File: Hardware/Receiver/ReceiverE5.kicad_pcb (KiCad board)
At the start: 2 copper layers, 41 parts, among them J1 KBUS, J2 AVR-PDI-6A, J3 CONN_01X08, J4 CONN_01X06, J5 CONN_01X06, J6 CONN_01X04, J7 CONN_01X04, U1 ATXMEGA32E5-A, U2 LM2731, U3 SN74LV07A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

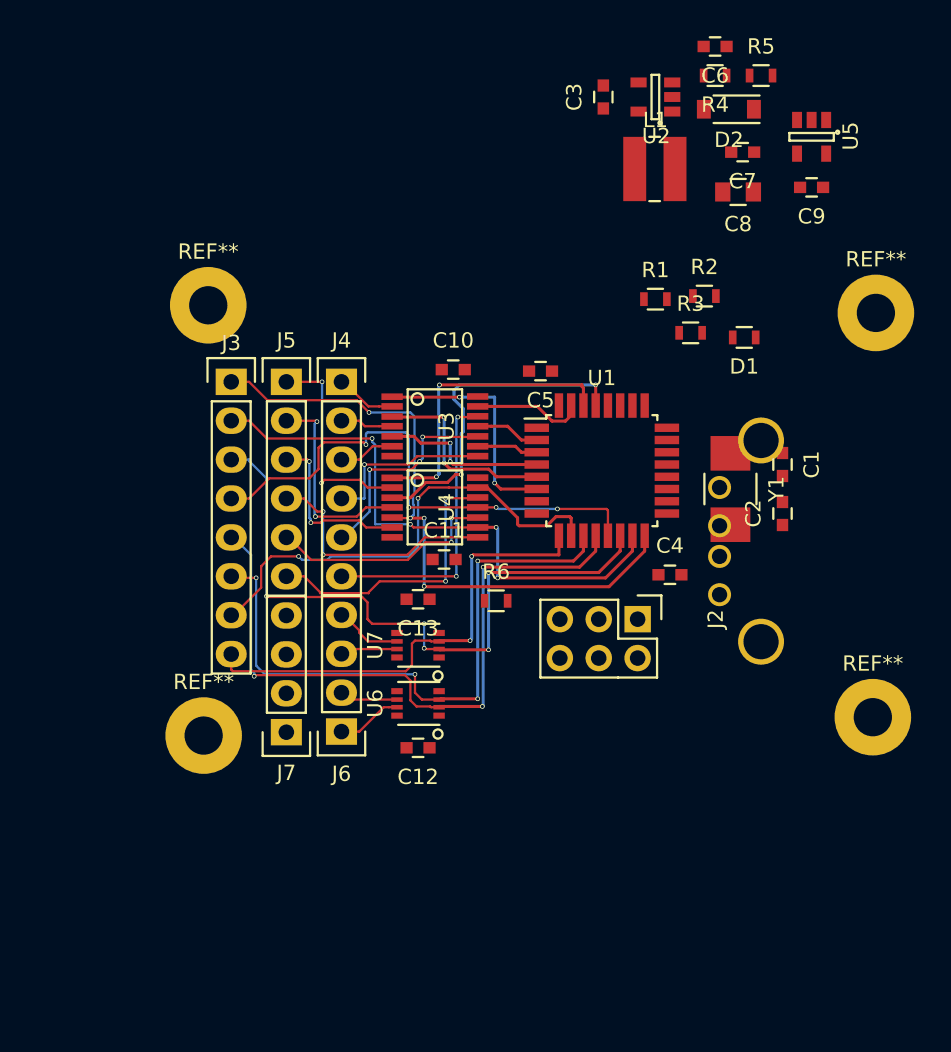
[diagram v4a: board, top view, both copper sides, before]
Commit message: 50x30mm layout
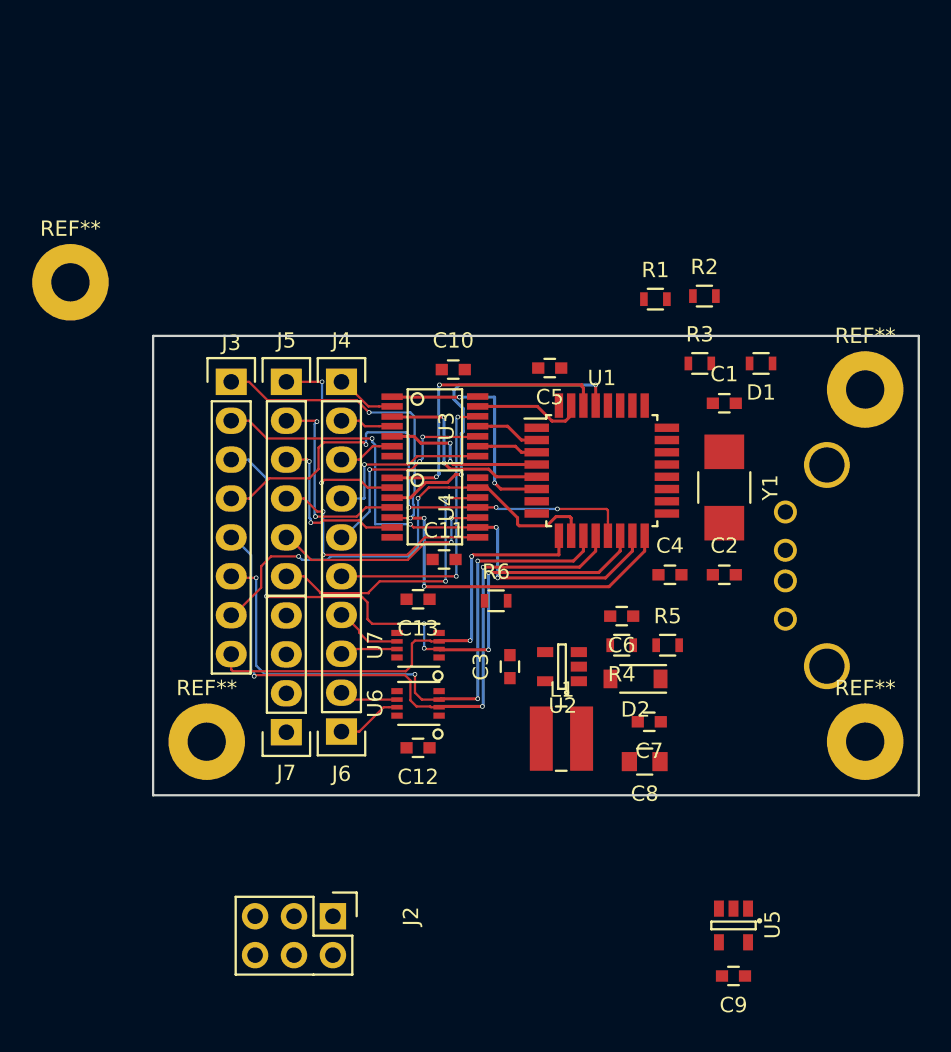
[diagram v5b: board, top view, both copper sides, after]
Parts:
- moved C9 51.8 mm to (104.9, 104.8)
- moved U5 51.8 mm to (104.9, 101.5)
- moved R4 37.7 mm to (97.6, 83.2)
- moved R5 37.7 mm to (100.6, 83.2)
- moved C3 37.7 mm to (90.3, 84.6)
- moved C6 37.7 mm to (97.6, 81.3)
- moved C7 37.7 mm to (99.4, 88.2)
- moved C8 37.7 mm to (99.1, 90.8)
- moved D2 37.7 mm to (98.5, 85.4)
- moved L1 37.7 mm to (93.7, 89.3)
- moved U2 37.7 mm to (93.7, 84.6)
- moved J2 27.8 mm to (78.7, 100.9)
- moved REF** 9.12 mm to (61.6, 59.5)
- moved C1 5.52 mm to (104.3, 67.4), turned to 0 degrees
- moved C2 5.52 mm to (104.3, 78.6), turned to 0 degrees
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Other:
- board outline added: 50 x 30 mm
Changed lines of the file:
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@@
     (area 0 0 0 0)
     (thickness 1.6)
-    (drawings 1)
+    (drawings 7)
     (tracks 369)
     (zones 0)
@@
   )
   (module Mounting_Holes:MountingHole_2.5mm_Pad (layer F.Cu)
-    (at 114.2 61.5)
+    (at 113.5 66.5)
     (descr "Mounting Hole 2.5mm")
     (tags "mounting hole 2.5mm")
@@
   )
   (module Mounting_Holes:MountingHole_2.5mm_Pad (layer F.Cu)
-    (at 114 87.9)
+    (at 113.5 89.5)
     (descr "Mounting Hole 2.5mm")
     (tags "mounting hole 2.5mm")
@@
   )
   (module Mounting_Holes:MountingHole_2.5mm_Pad (layer F.Cu)
-    (at 70.3 89.1)
+    (at 70.5 89.5)
     (descr "Mounting Hole 2.5mm")
     (tags "mounting hole 2.5mm")
@@
   )
   (module Capacitors_SMD:C_0603 (layer F.Cu)
-    (at 108.1 71.4 270)
+    (at 104.3 67.4)
     (descr "Capacitor SMD 0603, reflow soldering, AVX (see smccp.pdf)")
     (tags "capacitor 0603")
     (attr smd)
-    (fp_text reference C1 (at 0 -1.9 270) (layer F.SilkS)
-      (effects (font (size 1 1) (thickness 0.15)))
-    )
-    (fp_text value 22p (at 0 1.9 270) (layer F.Fab)
+    (fp_text reference C1 (at 0 -1.9) (layer F.SilkS)
+      (effects (font (size 1 1) (thickness 0.15)))
+    )
+    (fp_text value 22p (at 0 1.9) (layer F.Fab)
       (effects (font (size 1 1) (thickness 0.15)))
     )
@@
     (fp_line (start -0.35 -0.6) (end 0.35 -0.6) (layer F.SilkS) (width 0.15))
     (fp_line (start 0.35 0.6) (end -0.35 0.6) (layer F.SilkS) (width 0.15))
-    (pad 1 smd rect (at -0.75 0 270) (size 0.8 0.75) (layers F.Cu F.Paste F.Mask)
+    (pad 1 smd rect (at -0.75 0) (size 0.8 0.75) (layers F.Cu F.Paste F.Mask)
       (net 1 "Net-(C1-Pad1)"))
-    (pad 2 smd rect (at 0.75 0 270) (size 0.8 0.75) (layers F.Cu F.Paste F.Mask)
+    (pad 2 smd rect (at 0.75 0) (size 0.8 0.75) (layers F.Cu F.Paste F.Mask)
       (net 2 GND))
     (model Capacitors_SMD.3dshapes/C_0603.wrl
@@
   )
   (module Capacitors_SMD:C_0603 (layer F.Cu)
-    (at 108.1 74.6 90)
+    (at 104.3 78.6)
     (descr "Capacitor SMD 0603, reflow soldering, AVX (see smccp.pdf)")
     (tags "capacitor 0603")
     (attr smd)
-    (fp_text reference C2 (at 0 -1.9 90) (layer F.SilkS)
-      (effects (font (size 1 1) (thickness 0.15)))
-    )
-    (fp_text value 22p (at 0 1.9 90) (layer F.Fab)
+    (fp_text reference C2 (at 0 -1.9) (layer F.SilkS)
+      (effects (font (size 1 1) (thickness 0.15)))
+    )
+    (fp_text value 22p (at 0 1.9) (layer F.Fab)
       (effects (font (size 1 1) (thickness 0.15)))
     )
@@
     (fp_line (start -0.35 -0.6) (end 0.35 -0.6) (layer F.SilkS) (width 0.15))
     (fp_line (start 0.35 0.6) (end -0.35 0.6) (layer F.SilkS) (width 0.15))
-    (pad 1 smd rect (at -0.75 0 90) (size 0.8 0.75) (layers F.Cu F.Paste F.Mask)
+    (pad 1 smd rect (at -0.75 0) (size 0.8 0.75) (layers F.Cu F.Paste F.Mask)
       (net 3 "Net-(C2-Pad1)"))
-    (pad 2 smd rect (at 0.75 0 90) (size 0.8 0.75) (layers F.Cu F.Paste F.Mask)
+    (pad 2 smd rect (at 0.75 0) (size 0.8 0.75) (layers F.Cu F.Paste F.Mask)
       (net 2 GND))
     (model Capacitors_SMD.3dshapes/C_0603.wrl
@@
   )
   (module Capacitors_SMD:C_0603 (layer F.Cu)
-    (at 96.4 47.4 90)
+    (at 90.3 84.6 90)
     (descr "Capacitor SMD 0603, reflow soldering, AVX (see smccp.pdf)")
     (tags "capacitor 0603")
@@
   )
   (module Capacitors_SMD:C_0603 (layer F.Cu)
-    (at 92.3 65.3 180)
+    (at 92.9 65.1 180)
     (descr "Capacitor SMD 0603, reflow soldering, AVX (see smccp.pdf)")
     (tags "capacitor 0603")
@@
   )
   (module Capacitors_SMD:C_0603 (layer F.Cu)
-    (at 103.7 44.1 180)
+    (at 97.6 81.3 180)
     (descr "Capacitor SMD 0603, reflow soldering, AVX (see smccp.pdf)")
     (tags "capacitor 0603")
@@
   )
   (module Capacitors_SMD:C_0603 (layer F.Cu)
-    (at 105.5 51 180)
+    (at 99.4 88.2 180)
     (descr "Capacitor SMD 0603, reflow soldering, AVX (see smccp.pdf)")
     (tags "capacitor 0603")
@@
   )
   (module Capacitors_SMD:C_0805 (layer F.Cu)
-    (at 105.2 53.6 180)
+    (at 99.1 90.8 180)
     (descr "Capacitor SMD 0805, reflow soldering, AVX (see smccp.pdf)")
     (tags "capacitor 0805")
@@
   )
   (module Capacitors_SMD:C_0603 (layer F.Cu)
-    (at 110 53.3 180)
+    (at 104.9 104.8 180)
     (descr "Capacitor SMD 0603, reflow soldering, AVX (see smccp.pdf)")
     (tags "capacitor 0603")
@@
   )
   (module Resistors_SMD:R_0603 (layer F.Cu)
-    (at 105.6 63.1 180)
+    (at 106.7 64.8 180)
     (descr "Resistor SMD 0603, reflow soldering, Vishay (see dcrcw.pdf)")
     (tags "resistor 0603")
@@
   )
   (module Diodes_SMD:SOD-123 (layer F.Cu)
-    (at 104.6 48.2 180)
+    (at 98.5 85.4 180)
     (descr SOD-123)
     (tags SOD-123)
@@
   )
   (module kuro:USB_A_multicomp (layer B.Cu)
-    (at 106.7 76.4 270)
+    (at 111 78 270)
     (descr "FCI 87520")
     (tags "USB USB_A")
@@
   )
   (module Pin_Headers:Pin_Header_Straight_2x03 (layer F.Cu)
-    (at 98.64 81.5 270)
+    (at 78.74 100.9 270)
     (descr "Through hole pin header")
     (tags "pin header")
@@
   )
   (module kuro:SRN4012TA (layer F.Cu)
-    (at 99.8 52.1)
+    (at 93.7 89.3)
     (descr http://www.farnell.com/datasheets/2113222.pdf)
     (tags "Bournes inductor")
@@
   )
   (module Resistors_SMD:R_0603 (layer F.Cu)
-    (at 102.1 62.8)
+    (at 102.7 64.8)
     (descr "Resistor SMD 0603, reflow soldering, Vishay (see dcrcw.pdf)")
     (tags "resistor 0603")
@@
   )
   (module Resistors_SMD:R_0603 (layer F.Cu)
-    (at 103.7 46 180)
+    (at 97.6 83.2 180)
     (descr "Resistor SMD 0603, reflow soldering, Vishay (see dcrcw.pdf)")
     (tags "resistor 0603")
@@
   )
   (module Resistors_SMD:R_0603 (layer F.Cu)
-    (at 106.7 46)
+    (at 100.6 83.2)
     (descr "Resistor SMD 0603, reflow soldering, Vishay (see dcrcw.pdf)")
     (tags "resistor 0603")
@@
   )
   (module TO_SOT_Packages_SMD:SOT-23-5 (layer F.Cu)
-    (at 99.8 47.4 180)
+    (at 93.7 84.6 180)
     (descr "5-pin SOT23 package")
     (tags SOT-23-5)
@@
   )
   (module TO_SOT_Packages_SMD:SOT-23-5 (layer F.Cu)
-    (at 110 50 270)
+    (at 104.9 101.5 270)
     (descr "5-pin SOT23 package")
     (tags SOT-23-5)
@@
   )
   (module kuro:SMD_Crystal_Multi_QC6CB_7A_ABM7 (layer F.Cu)
-    (at 104.7 73 270)
+    (at 104.3 72.9 270)
     (descr "Multiple SMD crystal footprint.svg")
     (tags "QC6CB 7A ABM7")
@@
   )
   (module Mounting_Holes:MountingHole_2.5mm_Pad (layer F.Cu)
-    (at 70.6 61)
+    (at 61.6 59.5)
     (descr "Mounting Hole 2.5mm")
     (tags "mounting hole 2.5mm")
@@
     (pad 1 thru_hole circle (at 0 0) (size 5 5) (drill 2.5) (layers *.Cu *.Mask))
   )
-  (dimension 50 (width 0.3) (layer Eco1.User)
-    (gr_text "50.000 mm" (at 95.086733 49.844833) (layer Eco1.User)
+  (dimension 15 (width 0.3) (layer F.Fab)
+    (gr_text "15.000 mm" (at 122.017914 70.522279 270) (layer F.Fab)
       (effects (font (size 1.5 1.5) (thickness 0.3)))
     )
-    (feature1 (pts (xy 120.086733 49.844833) (xy 120.086733 49.844833)))
-    (feature2 (pts (xy 70.086733 49.844833) (xy 70.086733 49.844833)))
-    (crossbar (pts (xy 70.086733 49.844833) (xy 120.086733 49.844833)))
-    (arrow1a (pts (xy 120.086733 49.844833) (xy 118.960229 50.431254)))
-    (arrow1b (pts (xy 120.086733 49.844833) (xy 118.960229 49.258412)))
-    (arrow2a (pts (xy 70.086733 49.844833) (xy 71.213237 50.431254)))
-    (arrow2b (pts (xy 70.086733 49.844833) (xy 71.213237 49.258412)))
-  )
+    (feature1 (pts (xy 122.017914 78.022279) (xy 122.017914 78.022279)))
+    (feature2 (pts (xy 122.017914 63.022279) (xy 122.017914 63.022279)))
+    (crossbar (pts (xy 122.017914 63.022279) (xy 122.017914 78.022279)))
+    (arrow1a (pts (xy 122.017914 78.022279) (xy 121.431493 76.895775)))
+    (arrow1b (pts (xy 122.017914 78.022279) (xy 122.604335 76.895775)))
+    (arrow2a (pts (xy 122.017914 63.022279) (xy 121.431493 64.148783)))
+    (arrow2b (pts (xy 122.017914 63.022279) (xy 122.604335 64.148783)))
+  )
+  (dimension 30 (width 0.3) (layer F.Fab)
+    (gr_text "30.000 mm" (at 65 78 270) (layer F.Fab)
+      (effects (font (size 1.5 1.5) (thickness 0.3)))
+    )
+    (feature1 (pts (xy 65 93) (xy 65 93)))
+    (feature2 (pts (xy 65 63) (xy 65 63)))
+    (crossbar (pts (xy 65 63) (xy 65 93)))
+    (arrow1a (pts (xy 65 93) (xy 64.413579 91.873496)))
+    (arrow1b (pts (xy 65 93) (xy 65.586421 91.873496)))
+    (arrow2a (pts (xy 65 63) (xy 64.413579 64.126504)))
+    (arrow2b (pts (xy 65 63) (xy 65.586421 64.126504)))
+  )
+  (dimension 50 (width 0.3) (layer F.Fab)
+    (gr_text "50.000 mm" (at 92 61) (layer F.Fab)
+      (effects (font (size 1.5 1.5) (thickness 0.3)))
+    )
+    (feature1 (pts (xy 67 61) (xy 67 61)))
+    (feature2 (pts (xy 117 61) (xy 117 61)))
+    (crossbar (pts (xy 117 61) (xy 67 61)))
+    (arrow1a (pts (xy 67 61) (xy 68.126504 60.413579)))
+    (arrow1b (pts (xy 67 61) (xy 68.126504 61.586421)))
+    (arrow2a (pts (xy 117 61) (xy 115.873496 60.413579)))
+    (arrow2b (pts (xy 117 61) (xy 115.873496 61.586421)))
+  )
+  (gr_line (start 67 63) (end 67 93) (layer Edge.Cuts) (width 0.15))
+  (gr_line (start 117 63) (end 67 63) (layer Edge.Cuts) (width 0.15))
+  (gr_line (start 117 93) (end 117 63) (layer Edge.Cuts) (width 0.15))
+  (gr_line (start 67 93) (end 117 93) (layer Edge.Cuts) (width 0.15))
   (segment (start 84.7 74.9) (end 83.8 74.9) (width 0.2) (layer F.Cu) (net 15))
   (segment (start 84.7 79.35482) (end 84.7 74.9) (width 0.2) (layer B.Cu) (net 15))
